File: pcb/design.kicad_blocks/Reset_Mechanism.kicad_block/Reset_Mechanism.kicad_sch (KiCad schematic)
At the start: 4 parts, among them SW1 B3U-1000P

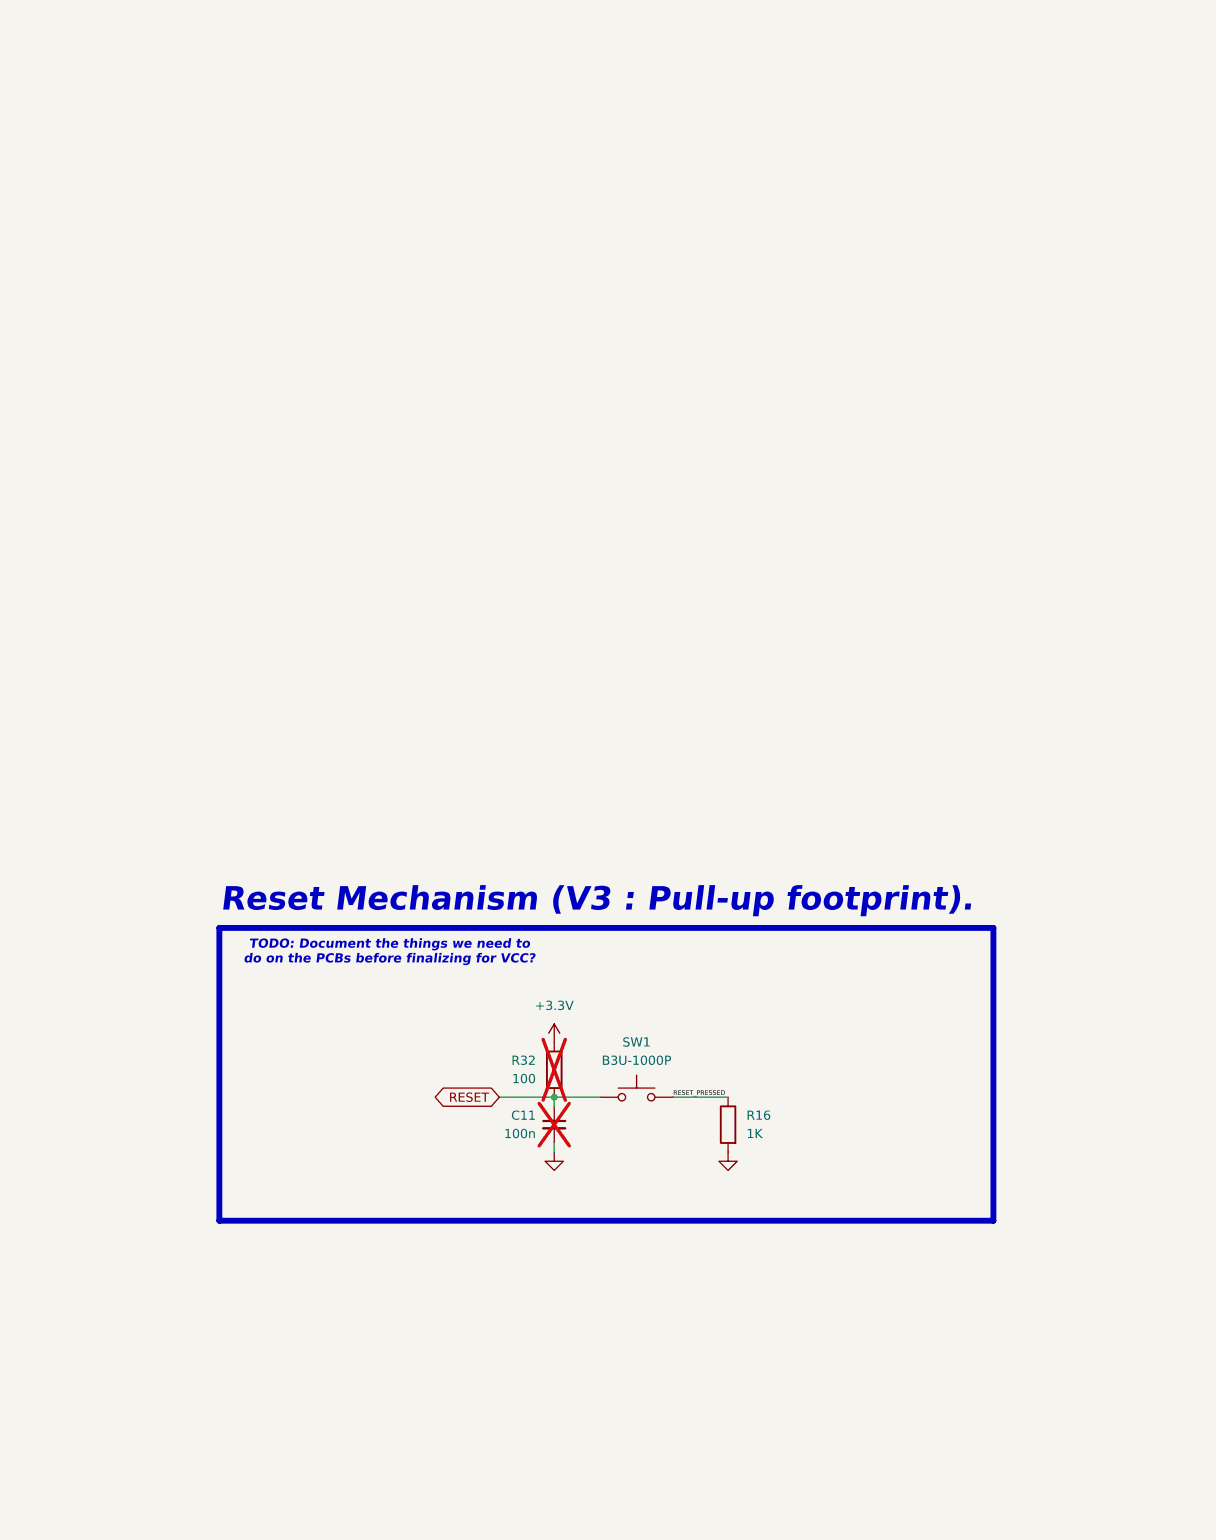
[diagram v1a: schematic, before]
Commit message: `Reset Mechanism (V4 : Removed local-net).`
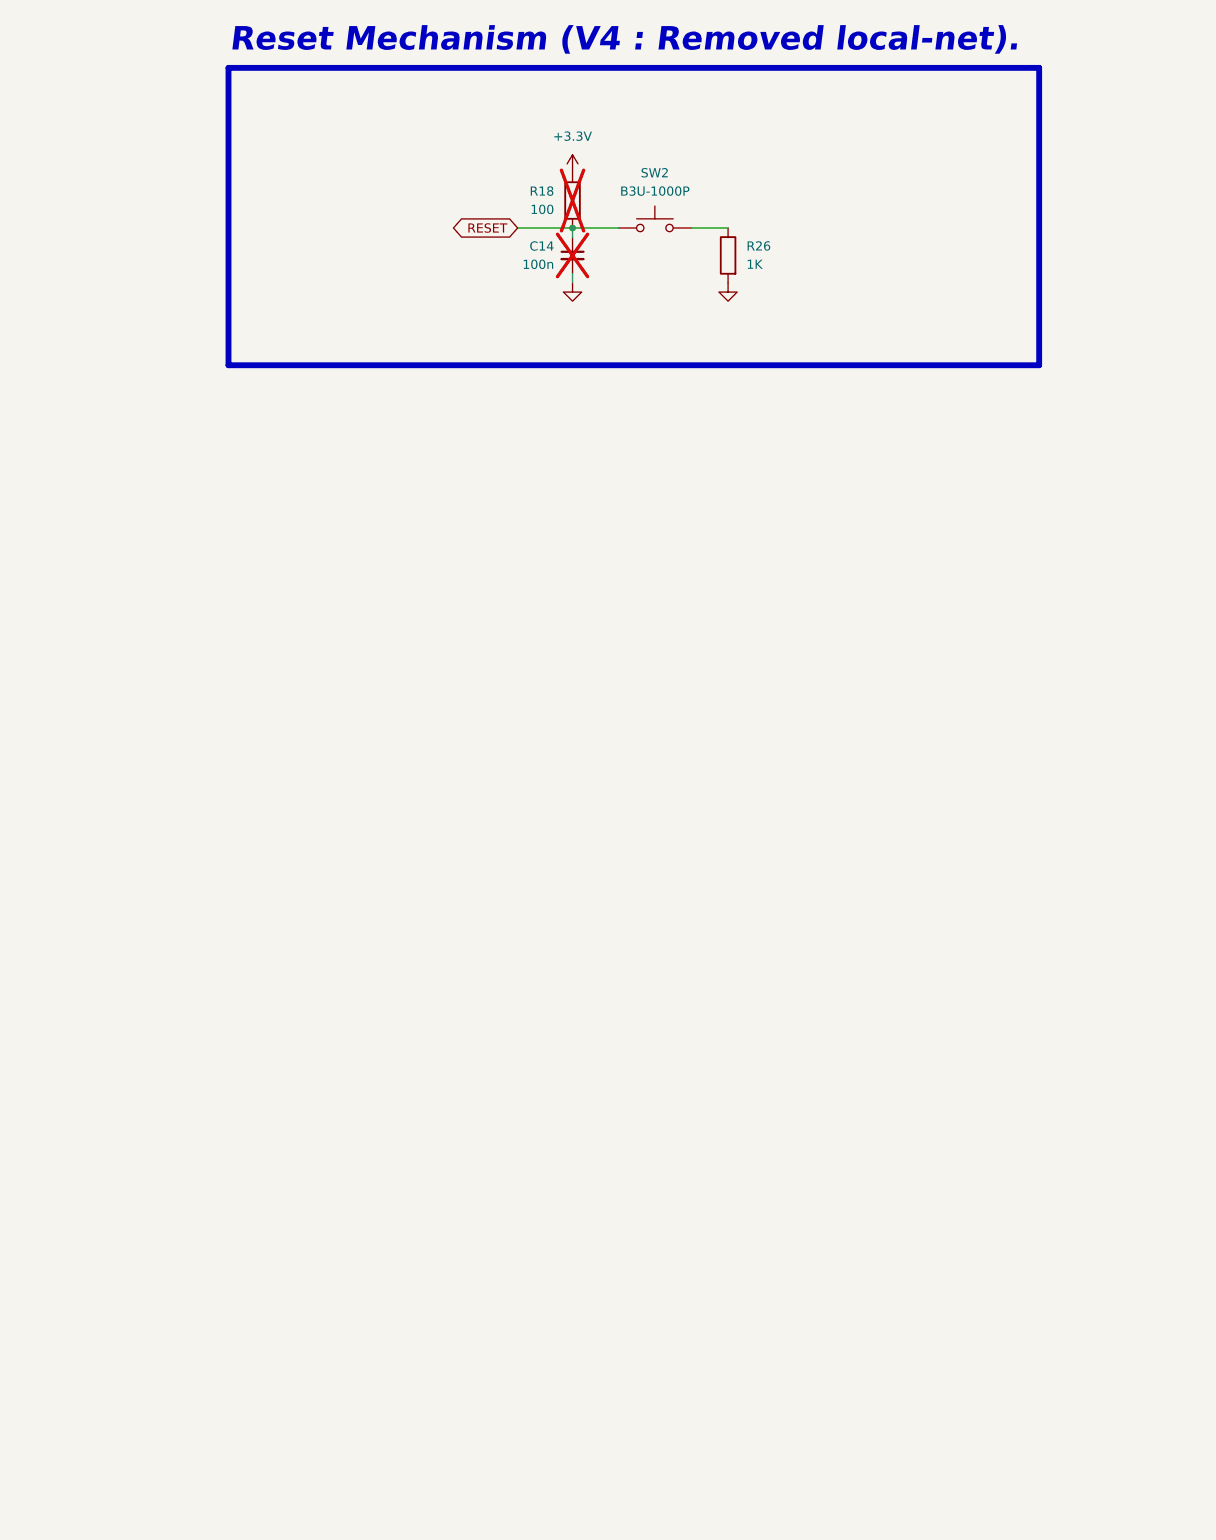
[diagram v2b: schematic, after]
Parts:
- renumbered C11 to C14, R32 to R18, R16 to R26, SW1 to SW2
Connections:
- net RESET_PRESSED: no longer names the net of R26.1, SW2.2
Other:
- note added: "Reset Mechanism (V4 : Removed local-net)."
- note removed: "Reset Mechanism (V3 : Pull-up footprint)."
- note removed: "TODO: Document the things we need to do on the PCBs before finalizing for VCC?"
- moved on the sheet: C14, R18, R26, SW2
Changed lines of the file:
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@@
 	(paper "A4")
 	(rectangle
-		(start 339.598 287.655)
-		(end 447.04 328.295)
+		(start 340.868 168.275)
+		(end 453.39 209.55)
 		(stroke
 			(width 0.8128)
@@
 		)
 	)
-	(text "Reset Mechanism (V3 : Pull-up footprint)."
-		(exclude_from_sim no)
-		(at 339.725 285.75 0)
+	(text "Reset Mechanism (V4 : Removed local-net)."
+		(exclude_from_sim no)
+		(at 340.995 166.37 0)
 		(effects
 			(font
@@
 		)
 	)
-	(text "TODO: Document the things we need to\ndo on the PCBs before finalizing for VCC?"
-		(exclude_from_sim no)
-		(at 363.22 291.084 0)
-		(effects
-			(font
-				(size 1.27 1.27)
-				(thickness 0.254)
-				(bold yes)
-				(italic yes)
-				(color 255 0 255 1)
-			)
-		)
-	)
 	(junction
-		(at 386.08 311.15)
+		(at 388.62 190.5)
 		(diameter 0)
 		(color 0 0 0 0)
@@
 	(wire
 		(pts
-			(xy 410.21 311.15) (xy 402.59 311.15)
+			(xy 410.21 190.5) (xy 405.13 190.5)
 		)
 		(stroke
@@
 	(wire
 		(pts
-			(xy 386.08 311.15) (xy 392.43 311.15)
+			(xy 388.62 190.5) (xy 394.97 190.5)
 		)
 		(stroke
@@
 	(wire
 		(pts
-			(xy 378.46 311.15) (xy 386.08 311.15)
+			(xy 381 190.5) (xy 388.62 190.5)
 		)
 		(stroke
@@
 	(wire
 		(pts
-			(xy 386.08 311.15) (xy 386.08 312.42)
+			(xy 388.62 190.5) (xy 388.62 191.77)
 		)
 		(stroke
@@
 	(wire
 		(pts
-			(xy 386.08 317.5) (xy 386.08 318.77)
+			(xy 388.62 196.85) (xy 388.62 198.12)
 		)
 		(stroke
@@
 		)
 	)
-	(label "RESET_PRESSED"
-		(at 402.59 311.15 0)
-		(effects
-			(font
-				(size 0.635 0.635)
-			)
-			(justify left bottom)
-		)
-	)
 	(global_label "RESET"
 		(shape bidirectional)
-		(at 378.46 311.15 180)
+		(at 381 190.5 180)
 		(fields_autoplaced yes)
 		(effects
@@
 		)
 		(property "Intersheetrefs" "${INTERSHEET_REFS}"
-			(at 368.6184 311.15 0)
+			(at 371.1584 190.5 0)
 			(effects
 				(font
@@
 	(symbol
 		(lib_id "Device:R")
-		(at 410.21 314.96 0)
+		(at 410.21 194.31 0)
 		(mirror y)
 		(unit 1)
@@
 		(dnp no)
 		(fields_autoplaced yes)
-		(property "Reference" "R16"
-			(at 412.75 313.6899 0)
+		(property "Reference" "R26"
+			(at 412.75 193.0399 0)
 			(effects
 				(font
@@
 		)
 		(property "Value" "1K"
-			(at 412.75 316.2299 0)
+			(at 412.75 195.5799 0)
 			(effects
 				(font
@@
 		)
 		(property "Footprint" "Resistor_SMD:R_1206_3216Metric_Pad1.30x1.75mm_HandSolder"
-			(at 411.988 314.96 90)
+			(at 411.988 194.31 90)
 			(effects
 				(font
@@
 		)
 		(property "Datasheet" "~"
-			(at 410.21 314.96 0)
+			(at 410.21 194.31 0)
 			(effects
 				(font
@@
 		)
 		(property "Description" "Resistor"
-			(at 410.21 314.96 0)
+			(at 410.21 194.31 0)
 			(effects
 				(font
@@
 			(project "MainFlightComputer"
 				(path "/0a179c33-cb18-4019-99e7-0e00d41f97d6"
-					(reference "R16")
+					(reference "R26")
 					(unit 1)
 				)
@@
 	(symbol
 		(lib_id "Device:C_Small")
-		(at 386.08 314.96 0)
+		(at 388.62 194.31 0)
 		(mirror y)
 		(unit 1)
@@
 		(on_board yes)
 		(dnp yes)
-		(property "Reference" "C11"
-			(at 383.54 313.6962 0)
+		(property "Reference" "C14"
+			(at 386.08 193.0462 0)
 			(effects
 				(font
@@
 		)
 		(property "Value" "100n"
-			(at 383.54 316.2362 0)
+			(at 386.08 195.5862 0)
 			(effects
 				(font
@@
 		)
 		(property "Footprint" "Capacitor_SMD:C_1206_3216Metric_Pad1.33x1.80mm_HandSolder"
-			(at 386.08 314.96 0)
+			(at 388.62 194.31 0)
 			(effects
 				(font
@@
 		)
 		(property "Datasheet" "~"
-			(at 386.08 314.96 0)
+			(at 388.62 194.31 0)
 			(effects
 				(font
@@
 		)
 		(property "Description" "Unpolarized capacitor, small symbol"
-			(at 386.08 314.96 0)
+			(at 388.62 194.31 0)
 			(effects
 				(font
@@
 			(project "MainFlightComputer"
 				(path "/0a179c33-cb18-4019-99e7-0e00d41f97d6"
-					(reference "C11")
+					(reference "C14")
 					(unit 1)
 				)
@@
 	(symbol
 		(lib_id "Switch:SW_Push")
-		(at 397.51 311.15 0)
+		(at 400.05 190.5 0)
 		(unit 1)
 		(exclude_from_sim no)
@@
 		(dnp no)
 		(fields_autoplaced yes)
-		(property "Reference" "SW1"
-			(at 397.51 303.53 0)
+		(property "Reference" "SW2"
+			(at 400.05 182.88 0)
 			(effects
 				(font
@@
 		)
 		(property "Value" "B3U-1000P"
-			(at 397.51 306.07 0)
+			(at 400.05 185.42 0)
 			(effects
 				(font
@@
 		)
 		(property "Footprint" "Button_Switch_SMD:SW_SPST_B3U-1000P"
-			(at 397.51 306.07 0)
+			(at 400.05 185.42 0)
 			(effects
 				(font
@@
 		)
 		(property "Datasheet" "~"
-			(at 397.51 306.07 0)
+			(at 400.05 185.42 0)
 			(effects
 				(font
@@
 		)
 		(property "Description" "Push button switch, generic, two pins"
-			(at 397.51 311.15 0)
+			(at 400.05 190.5 0)
 			(effects
 				(font
@@
 			(project ""
 				(path "/0a179c33-cb18-4019-99e7-0e00d41f97d6"
-					(reference "SW1")
+					(reference "SW2")
 					(unit 1)
 				)
@@
 	(symbol
 		(lib_id "power:GND")
-		(at 386.08 318.77 0)
+		(at 388.62 198.12 0)
 		(mirror y)
 		(unit 1)
@@
 		(dnp no)
 		(fields_autoplaced yes)
-		(property "Reference" "#PWR043"
-			(at 386.08 325.12 0)
+		(property "Reference" "#PWR041"
+			(at 388.62 204.47 0)
 			(effects
 				(font
@@
 		)
 		(property "Value" "GND"
-			(at 386.0799 322.58 90)
+			(at 388.6199 201.93 90)
 			(effects
 				(font
@@
 		)
 		(property "Footprint" ""
-			(at 386.08 318.77 0)
+			(at 388.62 198.12 0)
 			(effects
 				(font
@@
 		)
 		(property "Datasheet" ""
-			(at 386.08 318.77 0)
+			(at 388.62 198.12 0)
 			(effects
 				(font
@@
 		)
 		(property "Description" "Power symbol creates a global label with name \"GND\" , ground"
-			(at 386.08 318.77 0)
+			(at 388.62 198.12 0)
 			(effects
 				(font
@@
 			(project "MainFlightComputer"
 				(path "/0a179c33-cb18-4019-99e7-0e00d41f97d6"
-					(reference "#PWR043")
+					(reference "#PWR041")
 					(unit 1)
 				)
@@
 	(symbol
 		(lib_id "power:+3.3V")
-		(at 386.08 303.53 0)
+		(at 388.62 182.88 0)
 		(unit 1)
 		(exclude_from_sim no)
@@
 		(dnp no)
 		(fields_autoplaced yes)
-		(property "Reference" "#PWR044"
-			(at 386.08 307.34 0)
+		(property "Reference" "#PWR040"
+			(at 388.62 186.69 0)
 			(effects
 				(font
@@
 		)
 		(property "Value" "+3.3V"
-			(at 386.08 298.45 0)
+			(at 388.62 177.8 0)
 			(effects
 				(font
@@
 		)
 		(property "Footprint" ""
-			(at 386.08 303.53 0)
+			(at 388.62 182.88 0)
 			(effects
 				(font
@@
 		)
 		(property "Datasheet" ""
-			(at 386.08 303.53 0)
+			(at 388.62 182.88 0)
 			(effects
 				(font
@@
 		)
 		(property "Description" "Power symbol creates a global label with name \"+3.3V\""
-			(at 386.08 303.53 0)
+			(at 388.62 182.88 0)
 			(effects
 				(font
@@
 			(project "MainFlightComputer"
 				(path "/0a179c33-cb18-4019-99e7-0e00d41f97d6"
-					(reference "#PWR044")
+					(reference "#PWR040")
 					(unit 1)
 				)
@@
 	(symbol
 		(lib_id "Device:R")
-		(at 386.08 307.34 0)
+		(at 388.62 186.69 0)
 		(unit 1)
 		(exclude_from_sim no)
@@
 		(on_board yes)
 		(dnp yes)
-		(property "Reference" "R32"
-			(at 383.54 306.0699 0)
+		(property "Reference" "R18"
+			(at 386.08 185.4199 0)
 			(effects
 				(font
@@
 		)
 		(property "Value" "100"
-			(at 383.54 308.6099 0)
+			(at 386.08 187.9599 0)
 			(effects
 				(font
@@
 		)
 		(property "Footprint" "Resistor_SMD:R_1206_3216Metric_Pad1.30x1.75mm_HandSolder"
-			(at 384.302 307.34 90)
+			(at 386.842 186.69 90)
 			(effects
 				(font
@@
 		)
 		(property "Datasheet" "~"
-			(at 386.08 307.34 0)
+			(at 388.62 186.69 0)
 			(effects
 				(font
@@
 		)
 		(property "Description" "Resistor"
-			(at 386.08 307.34 0)
+			(at 388.62 186.69 0)
 			(effects
 				(font
@@
 			(project "MainFlightComputer"
 				(path "/0a179c33-cb18-4019-99e7-0e00d41f97d6"
-					(reference "R32")
+					(reference "R18")
 					(unit 1)
 				)
@@
 	(symbol
 		(lib_id "power:GND")
-		(at 410.21 318.77 0)
+		(at 410.21 198.12 0)
 		(mirror y)
 		(unit 1)
@@
 		(dnp no)
 		(fields_autoplaced yes)
-		(property "Reference" "#PWR042"
-			(at 410.21 325.12 0)
+		(property "Reference" "#PWR050"
+			(at 410.21 204.47 0)
 			(effects
 				(font
@@
 		)
 		(property "Value" "GND"
-			(at 410.2099 322.58 90)
+			(at 410.2099 201.93 90)
 			(effects
 				(font
@@
 		)
 		(property "Footprint" ""
-			(at 410.21 318.77 0)
+			(at 410.21 198.12 0)
 			(effects
 				(font
@@
 		)
 		(property "Datasheet" ""
-			(at 410.21 318.77 0)
+			(at 410.21 198.12 0)
 			(effects
 				(font
@@
 		)
 		(property "Description" "Power symbol creates a global label with name \"GND\" , ground"
-			(at 410.21 318.77 0)
+			(at 410.21 198.12 0)
 			(effects
 				(font
@@
 			(project "MainFlightComputer"
 				(path "/0a179c33-cb18-4019-99e7-0e00d41f97d6"
-					(reference "#PWR042")
-					(unit 1)
-				)
+					(reference "#PWR050")
+					(unit 1)
+				)
